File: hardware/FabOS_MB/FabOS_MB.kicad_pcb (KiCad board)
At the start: 4 copper layers, 68 x 68 mm, 116 parts, among them J201 USB_A, J301 RJ45, J401 USB_C_Receptacle, J601 Conn_ST_STDC14, SW601 boot, SW602 SW_Push, SW603 SW_Push, SW604 SW_Push, SW605 SW_Push, U201 NCV7329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

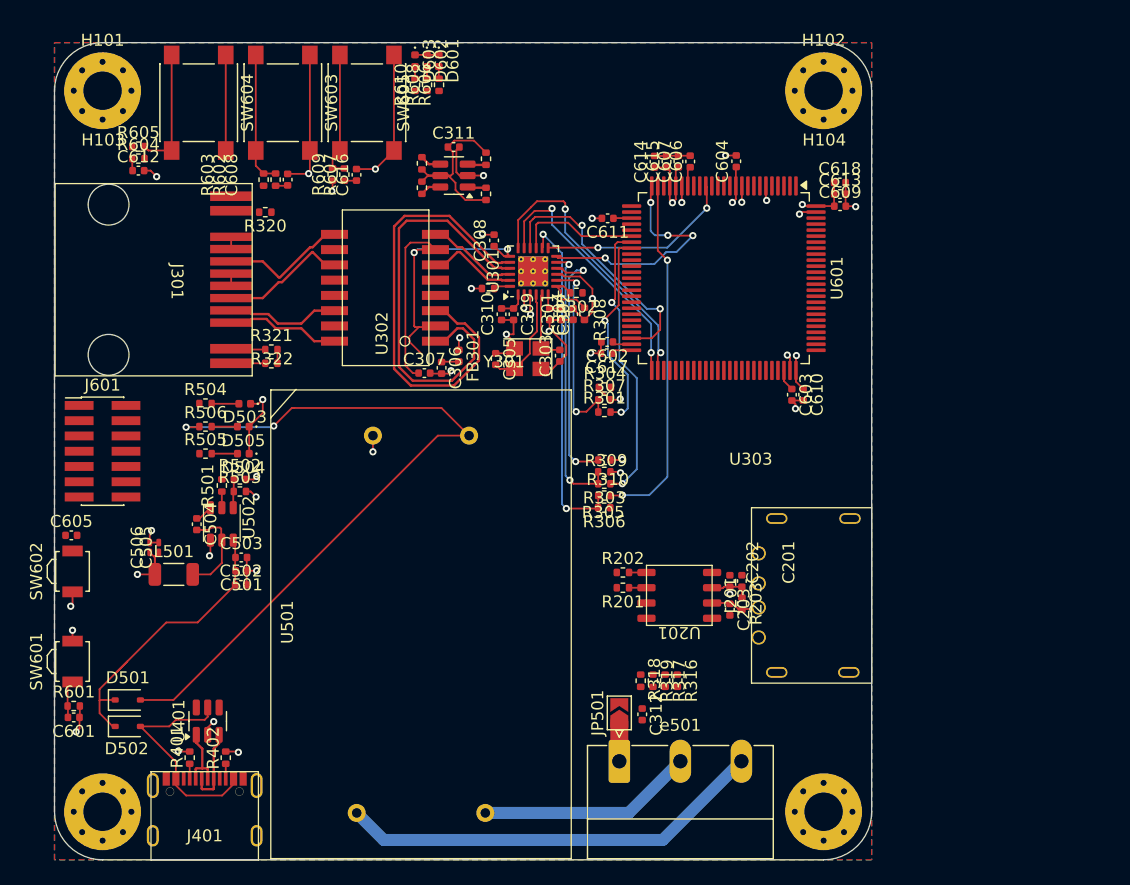
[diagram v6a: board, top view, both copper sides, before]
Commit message: update pcb
Tout les pins sont connectés. Il reste 32 violations à résoudre
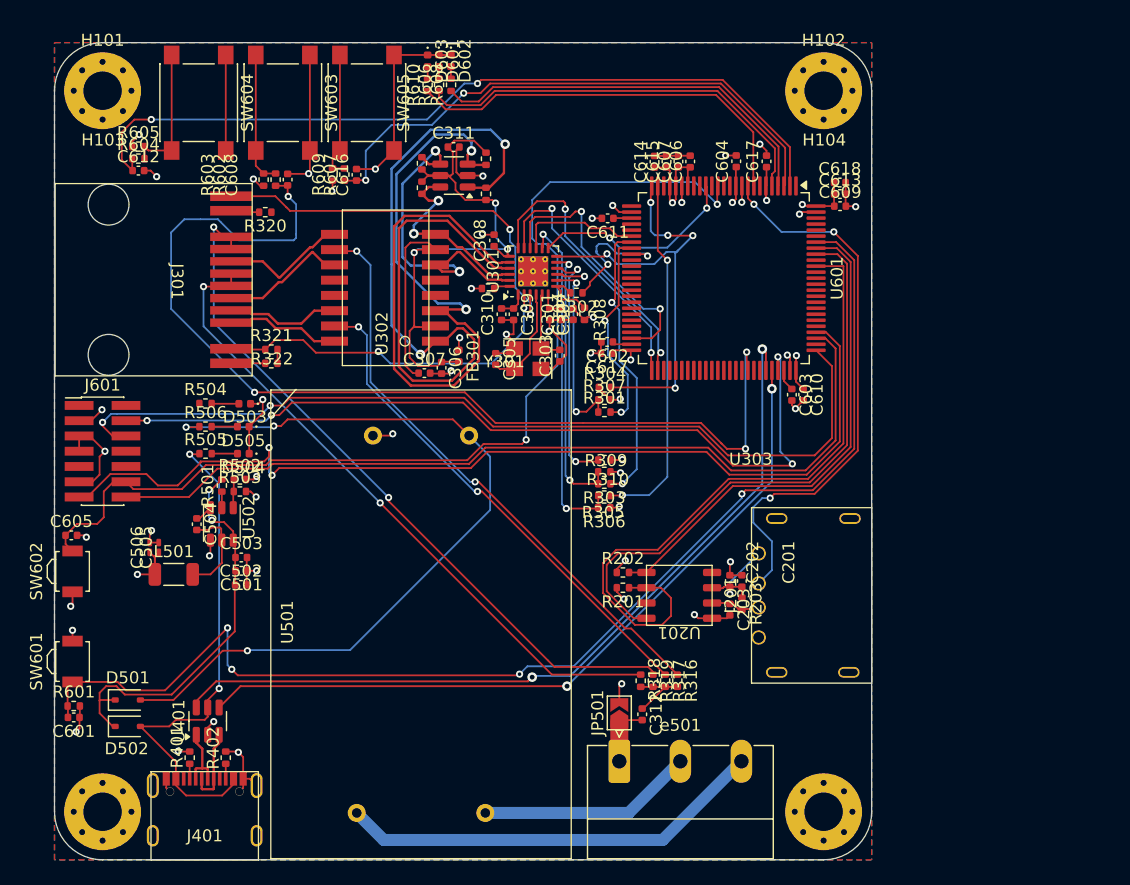
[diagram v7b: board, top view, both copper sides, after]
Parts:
- added C617: 100n, Capacitor_SMD:C_0402_1005Metric, F.Cu at (155.2, 105.9)
- moved D602 2.00 mm to (129.0, 97.5)
- moved R608 2.00 mm to (129.0, 99.5)
- moved D603 1.05 mm to (127.0, 97.5)
- moved R610 1.05 mm to (127.0, 99.5)
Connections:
- U601 pad 93: /USART1_TX -> /USART1_RX
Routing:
- net Net-(U601-BOOT0): track 3.13 -> 101.6 mm, vias 0 -> 4
- net /STM32/NRST: track 0.00 -> 85.6 mm, vias 0 -> 2
- net /STM32/BTN1: track 1.01 -> 86.0 mm, vias 0 -> 4
- net /STM32/VCP_RX: track 0.00 -> 81.6 mm, vias 0 -> 2
- net /STM32/SWCLK: track 0.00 -> 74.6 mm, vias 0 -> 2
- net /STM32/VCP_TX: track 0.00 -> 72.2 mm
- net /STM32/SWDIO: track 0.00 -> 68.8 mm, vias 0 -> 4
- net /USB_DM: track 0.00 -> 68.2 mm, vias 0 -> 2
- net /STM32/BTN2: track 1.01 -> 67.5 mm, vias 0 -> 2
- net /USB_DP: track 0.00 -> 63.0 mm, vias 0 -> 2
- net Net-(J301-Pad7): track 1.02 -> 59.8 mm, vias 0 -> 2
- net /LIN_EN: track 1.45 -> 56.0 mm
- net Net-(J301-Pad4): track 1.02 -> 55.0 mm, vias 0 -> 2
- net /ethernet/RXCT: track 0.00 -> 48.9 mm, vias 0 -> 2
- net /USART1_TX: track 0.00 -> 48.6 mm
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
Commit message: update
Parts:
- moved D603 0.10 mm to (127.0, 97.5)
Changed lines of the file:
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@@
 	(footprint "Diode_SMD:D_0402_1005Metric"
 		(layer "F.Cu")
-		(at 127.05 97.515 -90)
+		(at 126.95 97.515 -90)
 		(descr "Diode SMD 0402 (1005 Metric), square (rectangular) end terminal, IPC_7351 nominal, (Body size source: http://www.tortai-tech.com/upload/download/2011102023233369053.pdf), generated with kicad-footprint-generator")
 		(tags "diode")
@@
 	)
 	(segment
+		(start 156.95 121.9)
+		(end 157.2 122.15)
+		(width 0.15)
+		(layer "F.Cu")
+		(net 2)
+	)
+	(segment
 		(start 129.693749 104.6875)
 		(end 129.441749 104.9395)
@@
 	)
 	(segment
-		(start 157.2 123.275)
-		(end 157.2 122.22)
-		(width 0.15)
-		(layer "F.Cu")
-		(net 2)
-	)
-	(segment
 		(start 107.25 154.99)
 		(end 106.34 154.99)
@@
 	)
 	(segment
+		(start 157.2 122.15)
+		(end 157.2 123.275)
+		(width 0.15)
+		(layer "F.Cu")
+		(net 2)
+	)
+	(segment
 		(start 153.2 107.925)
 		(end 153.2 109.27)
@@
 	)
 	(segment
-		(start 157.2 122.22)
-		(end 156.98 122)
-		(width 0.15)
-		(layer "F.Cu")
-		(net 2)
-	)
-	(segment
 		(start 143 149.55)
 		(end 143.2 149.35)
@@
 	)
 	(via
-		(at 156.98 122)
+		(at 156.95 121.9)
 		(size 0.6)
 		(drill 0.3)
@@
 			)
 		)
+	)
+	(zone
+		(net 2)
+		(net_name "GND")
+		(layer "In1.Cu")
+		(hatch edge 0.5)
+		(priority 3)
+		(connect_pads
+			(clearance 0.5)
+		)
+		(min_thickness 0.25)
+		(filled_areas_thickness no)
+		(fill yes
+			(thermal_gap 0.5)
+			(thermal_bridge_width 0.5)
+		)
+		(polygon
+			(pts
+				(xy 96 96) (xy 96 164) (xy 164 164) (xy 164 96)
+			)
+		)
